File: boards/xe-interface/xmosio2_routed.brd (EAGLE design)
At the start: 116.8 x 55.2 mm, 105 parts, among them IC1 IDTQS3245QSOP20, IC2 IDTQS3245QSOP20, IC3 IDTQS3245QSOP20, IC4 IDTQS3245QSOP20, IC5 IDTQS3245QSOP20, U1 24 MHz Osc. (F535L-24), U2 USD-SOCKETNEW, X1 0446200002

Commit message: Latest board (routed and unrolled)
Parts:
- added GPIO: (no value), pinhead:1X04
- added H1, H2, H3, H4: MOUNT-HOLE3.2, holes:3,2
- added LED2: ok33, led:CHIP-LED0805
- added MEM_SEL: (no value), special:EDG-02
- added PBI_ID: (no value), special:EDG-03
- added R28: 47R, rcl:R1206
- added R29, R30, R31, R33, R34: 10K, rcl:R1206
- added SJ2, SJ3: SOLDERJUMPERNO, SparkFun:SJ_2S-NO
- added U$19: XE_SLOT, pbxl:XE_SLOT
- C1, C2, C3, C4, C5: device rcl:C0805 -> rcl:C1206
- C10, C11, C12, C13, C14, C15, C16, C17, C18, C19, C20, C21, C22, C23, C24, C25, C26, C28, C31, C34, C35, C36, C37, C38, C39, C40, C41, C42, C43, C44, C45, C46, C6, C7, C8, C9: device rcl:C0603 -> rcl:C1206
- R1, R10, R11, R12, R13, R14, R15, R16, R17, R18, R19, R2, R20, R21, R22, R23, R24, R25, R26, R27, R3, R4, R5, R6, R7, R8, R9: device rcl:R0603 -> rcl:R1206
- moved DBG3 116.3 mm to (113.7, 69.8), turned to 90 degrees
- moved DBG2 115.9 mm to (113.7, 66.7), turned to 90 degrees
- moved DBG1 115.6 mm to (113.7, 63.5), turned to 90 degrees
- moved DBG0 115.2 mm to (113.7, 60.3), turned to 90 degrees
- moved R23 101.1 mm to (108.6, 69.8), turned to 180 degrees
- moved R22 97.4 mm to (108.6, 66.7), turned to 180 degrees
- moved R21 93.8 mm to (108.6, 63.5), turned to 180 degrees
- moved U$10 93.7 mm to (23.9, 54.1), turned to 90 degrees
- moved R10 93.4 mm to (23.4, 59.9), turned to 0 degrees
- moved R20 90.1 mm to (108.6, 60.3), turned to 180 degrees
- moved U$9 87.2 mm to (34.2, 51.5), turned to 90 degrees
- moved R11 86.4 mm to (23.4, 47.9), turned to 0 degrees
- moved R8 79.8 mm to (22.6, 38.6), turned to 90 degrees
- moved C40 77.3 mm to (22.6, 31.7), turned to 90 degrees
- moved C39 76.1 mm to (22.6, 23.4), turned to 270 degrees
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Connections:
- new net N$30: C29.+, L1.1, LED1.A, R3.2, SJ2.1
- new net N$31: LED2.C, R28.2
- new net N$32: C32.+, L2.1, LED2.A, R6.2, SJ3.1
- new net N$34: MEM_SEL.2, R29.1, U$2.25
- new net N$35: MEM_SEL.1, R30.2, U$2.26
- new net N$36: GPIO.3, U$2.12
- new net N$37: GPIO.2, U$2.14
- new net PBI0: PBI_ID.1, R31.2, U$2.33
- new net PBI1: PBI_ID.2, R34.2, U$2.61
- new net PBI2: PBI_ID.3, R33.2, U$2.62
- net +5V: now also U$19.26, U$19.44
- net B1: now also U$19.1
- net B10: now also U$19.11
- net B11: now also U$19.12
- net B12: now also U$19.13
- net B13: now also U$19.14
- net B14: now also U$19.15
- net B15: now also U$19.16
- net B16: now also U$19.17
- net B17: now also U$19.18
- net B18: now also U$19.19
- net B19: now also U$19.20
- net B2: now also U$19.2
- net B20: now also U$19.21
- net B21: now also U$19.22
- net B22: now also U$19.23
- net B23: now also U$19.24
- net B24: now also U$19.25
- net B25: now also U$19.27
- net B26: now also U$19.28
- net B27: now also U$19.29
- net B28: now also U$19.30
- net B29: now also U$19.32
- net B3: now also U$19.4
- net B30: now also U$19.33
- net B31: now also U$19.34
- net B32: now also U$19.35
- net B33: now also U$19.36
- net B34: now also U$19.37
- net B35: now also U$19.38
- net B36: now also U$19.39
- net B37: now also U$19.41
- net B38: now also U$19.42
- net B4: now also U$19.5
- net B5: now also U$19.6
- net B6: now also U$19.7
- net B7: now also U$19.8
- net B8: now also U$19.9
- net B9: now also U$19.10
- net GND: now also GPIO.1, R28.1, R29.2, R30.1, R31.1, R33.1, R34.1, U$19.3, U$19.43
- net VCCINT: now also SJ3.2; no longer C32.+, L2.1, R6.2, U$6.5
- net VCCIO: now also GPIO.4, MEM_SEL.3, MEM_SEL.4, PBI_ID.4, PBI_ID.5, PBI_ID.6, SJ2.2, U$6.5; no longer C29.+, L1.1, LED1.A, R3.2
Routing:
- net VCCIO: track 456.0 -> 256.4 mm, vias 10 -> 29
- net +5V: track 145.0 -> 238.6 mm, vias 1 -> 2
- net SDC_D1: track 64.5 -> 155.1 mm
- net GND: track 464.6 -> 551.5 mm, vias 32 -> 37
- net SDC_CLK: track 69.7 -> 147.2 mm
- net N$33: track 23.3 -> 99.8 mm, vias 1 -> 3
- net N$21: track 22.1 -> 96.7 mm, vias 1 -> 0
- net N$35: track 0.00 -> 74.3 mm, vias 0 -> 3
- net N$36: track 0.00 -> 70.2 mm, vias 0 -> 1
- net N$34: track 0.00 -> 62.0 mm, vias 0 -> 1
- net PBI2: track 0.00 -> 61.1 mm, vias 0 -> 1
- net N$32: track 0.00 -> 56.3 mm
- net VCCINT: track 174.3 -> 228.8 mm, vias 10 -> 4
- net PBI0: track 0.00 -> 54.4 mm, vias 0 -> 1
- net N$30: track 0.00 -> 52.6 mm
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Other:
- board size 116.8 x 55.2 mm -> 116.8 x 100 mm
- board text added: "(c) 2018 SjG"
- board text added: "+1v"
- board text added: "+3.3v"
- board text added: "+5v"
- board text added: "3.3V"
- board text added: "GND"
- board text added: "PGOOD"
- board text added: "XMOS io v2.0"

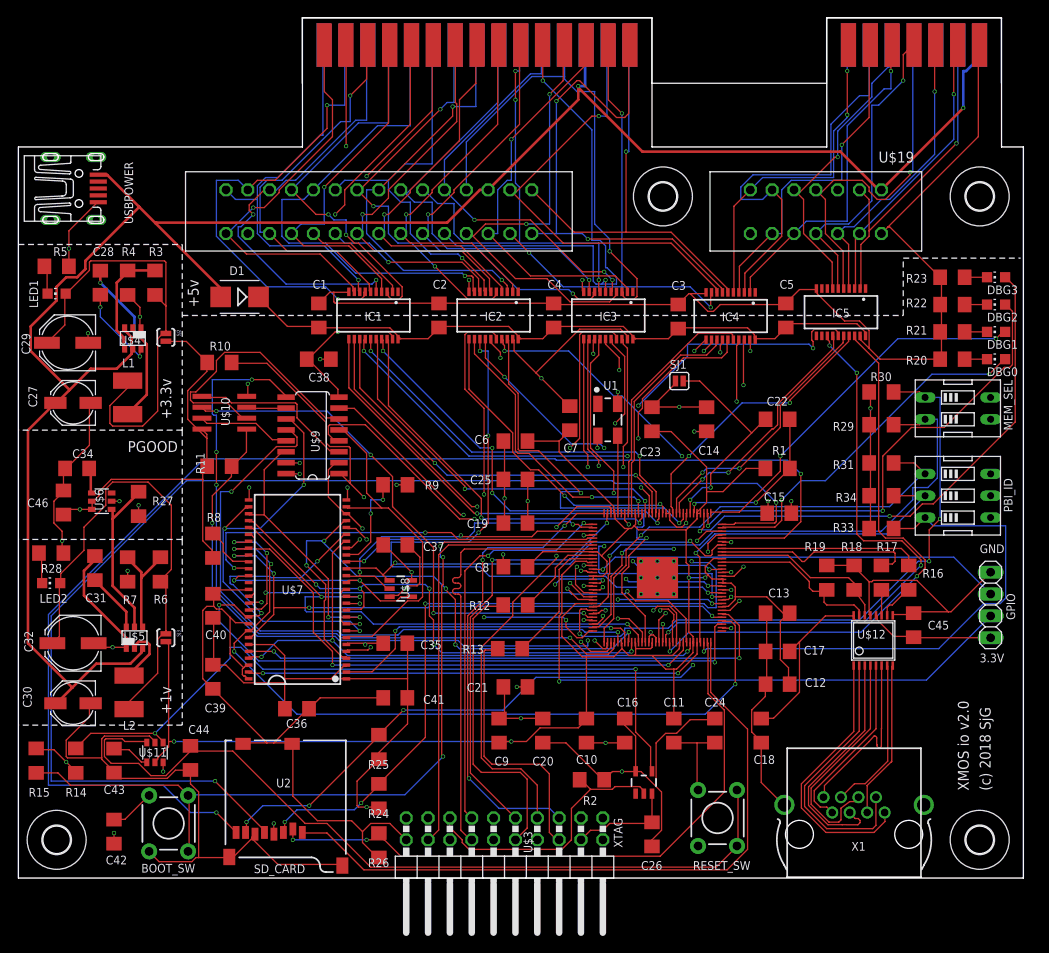
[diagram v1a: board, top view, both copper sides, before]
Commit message: Latest design changes  - Move the XTAG connector back significantly, so the shroud is not overhanging the board  - Use the SD card slot, not the micro-SD card, it’s easier to solder  - Fix the SD card pinouts  - Remove an unwanted pull-up on the SD card
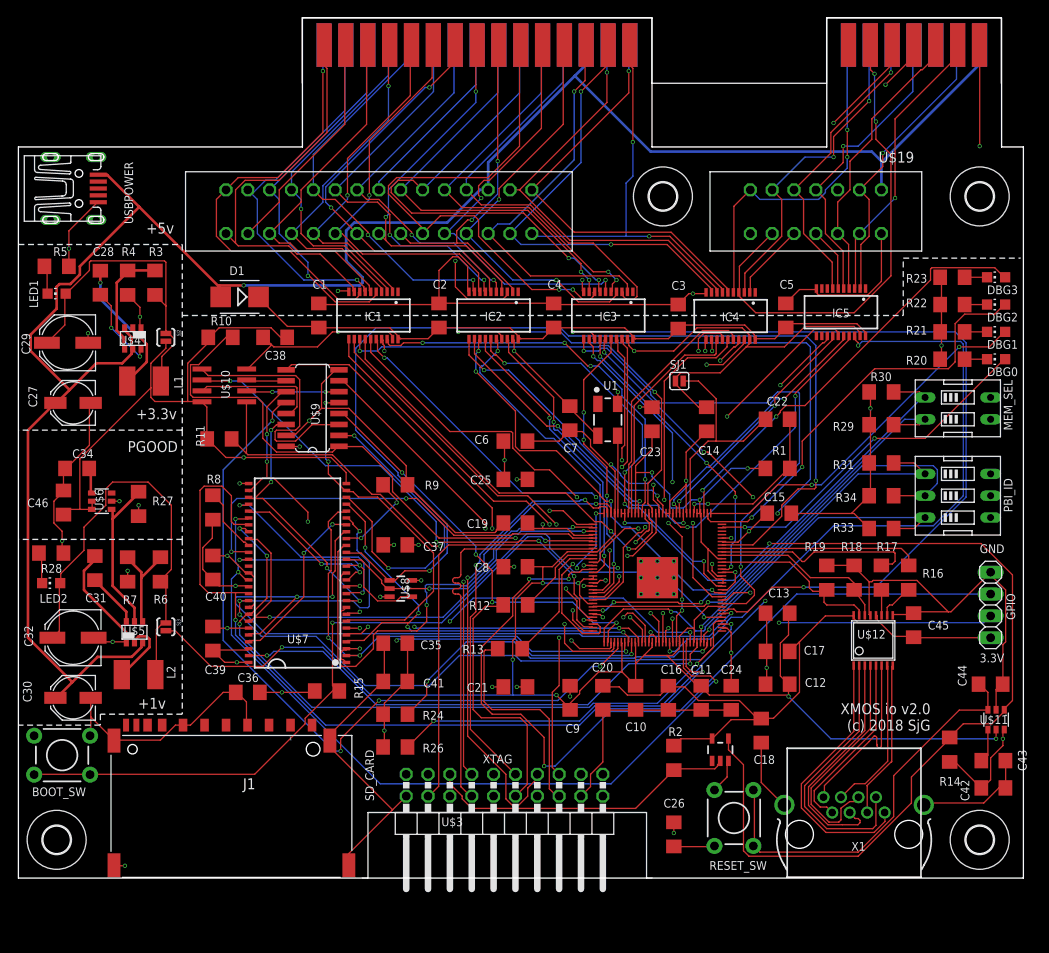
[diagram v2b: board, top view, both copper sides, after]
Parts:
- removed R25: 10K, rcl:R1206
- removed U2: USD-SOCKETNEW, SparkFun-Connectors:MICRO-SD-SOCKET-PP
- added J1: (no value), InputOutputIO (rev17e):693063020911
- moved C42 102.4 mm to (113.3, 10.5), turned to 0 degrees
- moved C43 102.2 mm to (113.3, 13.7), turned to 0 degrees
- moved R14 101.6 mm to (108.3, 14.9)
- moved U$11 97.9 mm to (113.7, 18.4)
- moved C44 93.4 mm to (113.0, 22.5), turned to 180 degrees
- moved R15 34.8 mm to (35.9, 21.7), turned to 180 degrees
- moved BOOT_SW 14.7 mm to (5.08, 14.3), turned to 180 degrees
- moved R26 11.6 mm to (43.8, 15.2), turned to 0 degrees
- moved R2 9.86 mm to (76.2, 14.0), turned to 90 degrees
- moved R24 9.71 mm to (43.8, 19.1), turned to 180 degrees
- moved U$3 9.67 mm to (81.6, 14.9)
- moved C9 9.09 mm to (64.1, 21.0)
- moved C20 7.96 mm to (67.9, 21.0), turned to 270 degrees
- moved C10 6.87 mm to (71.8, 21.0)
- moved C16 6.35 mm to (75.6, 21.0)
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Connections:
- new net SDC_CD: U$2.84
- net GND: now also J1.3, J1.6, J1.GND1, J1.GND2, J1.GND3, J1.GND4; no longer R26.2, U2.6, U2.CD1, U2.CD2, U2.GND1, U2.GND3
- net SDC_CLK: now also U$2.64; no longer U$2.96, U2.5
- net SDC_CMD: now also U$2.63; no longer U$2.94, U2.3
- net SDC_D0: now also U$2.96; no longer R25.1, U$2.93, U2.7
- net SDC_D1: now also U$2.94; no longer U$2.92, U2.8
- net SDC_D2: now also U$2.93; no longer U$2.64, U2.1
- net SDC_D3: now also R26.2, U$2.92; no longer R26.1, U$2.63, U2.2
- net VCCIO: now also R26.1; no longer R25.2, U2.4
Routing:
- net SDC_D1: track 155.1 -> 0.00 mm, vias 2 -> 0
- net SDC_CLK: track 147.2 -> 0.00 mm, vias 2 -> 0
- net !SD_CAS!: track 48.3 -> 128.9 mm
- net SDC_D2: track 80.4 -> 0.00 mm
- net SDC_D0: track 77.7 -> 0.00 mm, vias 5 -> 0
- net X_D0: track 40.0 -> 101.4 mm
- net N$21: track 96.7 -> 47.4 mm
- net N$37: track 48.6 -> 97.4 mm, vias 1 -> 3
- net SDC_CMD: track 85.1 -> 41.1 mm, vias 5 -> 2
- net X_D2: track 47.2 -> 82.4 mm
- net X_D4: track 77.0 -> 46.8 mm
- net SD_ADQ9: track 67.8 -> 97.6 mm, vias 4 -> 2
- net SD_ADQ4/QS_D2: track 84.7 -> 57.7 mm, vias 4 -> 2
- net VCCINT: track 228.8 -> 254.1 mm, vias 4 -> 11
- net PBI2: track 61.1 -> 36.6 mm
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
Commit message: Add a new progress post
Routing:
- net !SD_CAS!: track 128.9 -> 49.6 mm, vias 2 -> 3
- net X_RD4: track 54.6 -> 120.7 mm
- net X_D0: track 101.4 -> 43.8 mm
- net VCCINT: track 254.1 -> 305.2 mm, vias 11 -> 16
- net N$34: track 51.6 -> 102.2 mm
- net !X_S4!: track 51.9 -> 99.3 mm
- net N$37: track 97.4 -> 52.5 mm, vias 3 -> 1
- net X_D2: track 82.4 -> 43.5 mm, vias 3 -> 2
- net !RESET!: track 122.3 -> 87.7 mm
- net VCCIO: track 272.5 -> 244.3 mm, vias 24 -> 30
- net X_A8: track 33.7 -> 61.6 mm
- net SD_ADQ8: track 93.0 -> 68.3 mm, vias 3 -> 2
- net X_D1: track 61.1 -> 39.3 mm
- net SD_ADQ5/QS_D3: track 88.7 -> 67.7 mm, vias 4 -> 2
- net QSPI_CLK: track 60.3 -> 81.2 mm, vias 4 -> 2
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
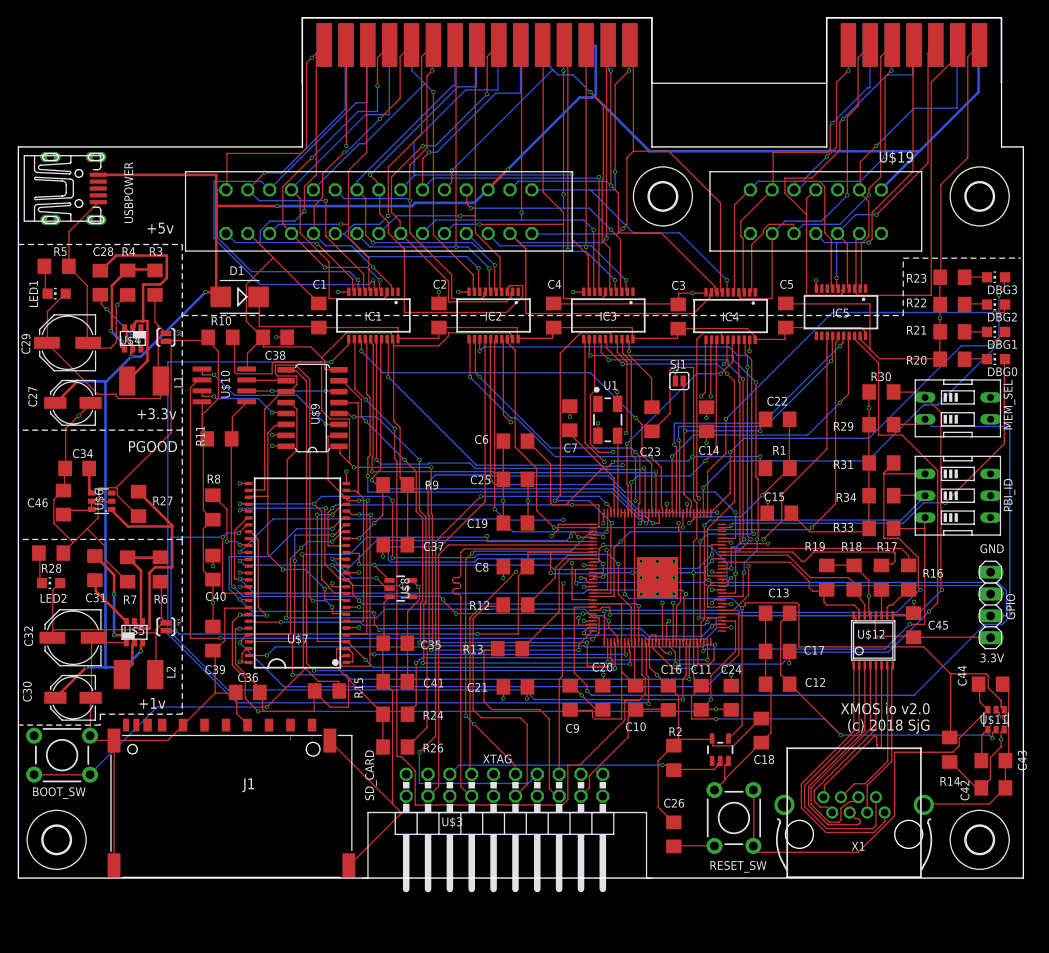
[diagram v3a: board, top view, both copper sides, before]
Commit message: Update the routed and unrouted board files, delete an unwanted routed-board file
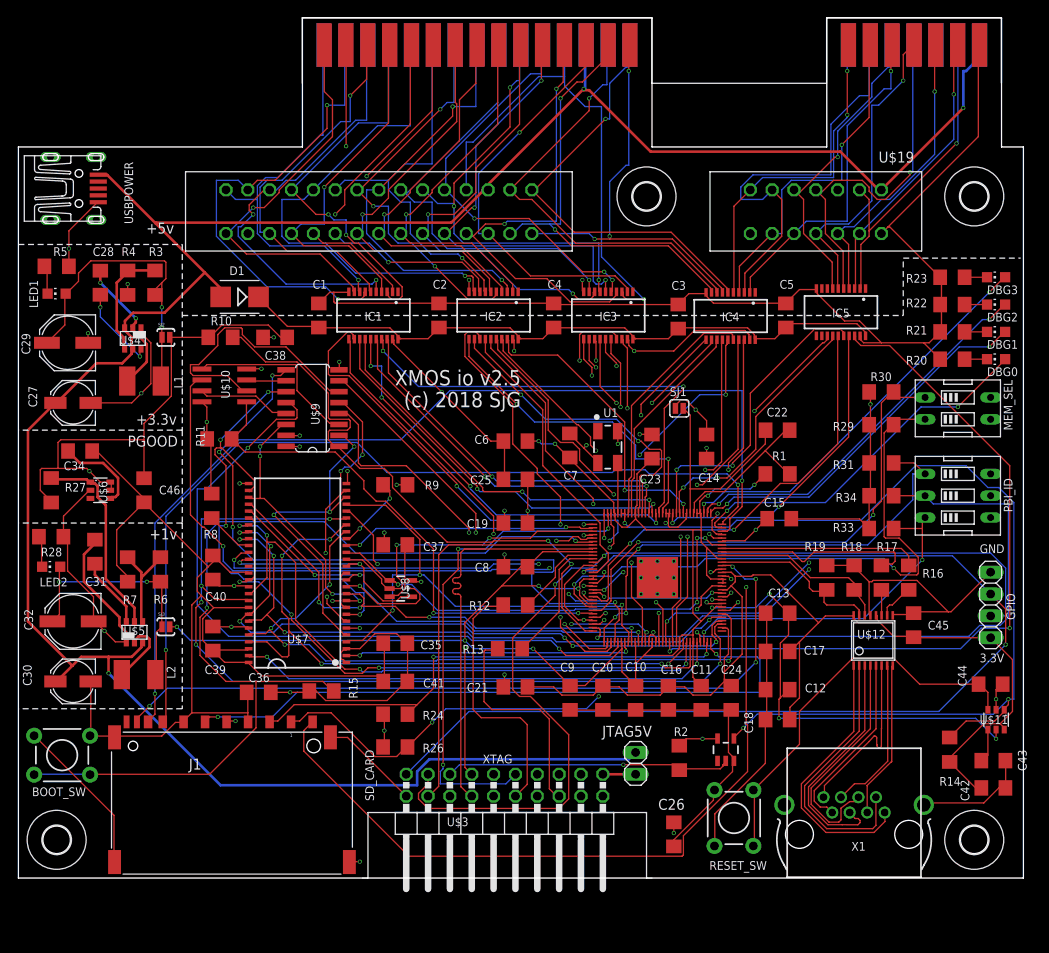
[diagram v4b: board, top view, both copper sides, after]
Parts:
- added JTAG5V: PSU, pinhead:1X02
- GPIO: value (none) -> UART
- J1: value (none) -> SD_CARD
- MEM_SEL: value (none) -> CT2092MS-ND
- PBI_ID: value (none) -> CT2093MS-ND
- moved R27 10.3 mm to (3.81, 45.1)
- moved C46 9.47 mm to (14.6, 45.1), turned to 270 degrees
- moved C14 3.18 mm to (80.0, 50.2)
- moved C23 3.18 mm to (73.7, 50.2)
- moved C7 3.17 mm to (64.1, 50.3)
- moved SJ1 3.17 mm to (76.8, 54.6)
- moved U1 3.17 mm to (68.5, 50.1)
- moved C18 2.29 mm to (88.3, 18.4), turned to 180 degrees
- moved C34 2.05 mm to (7.17, 49.6), turned to 0 degrees
- moved C30 1.91 mm to (6.35, 22.9)
- moved H3 1.91 mm to (73.0, 79.2)
- moved LED2 1.91 mm to (3.81, 36.2)
- moved R28 1.91 mm to (3.81, 39.7)
- moved C32 1.90 mm to (6.35, 29.8)
- moved C31 1.90 mm to (8.89, 37.9)
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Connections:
- net N$21 renamed TRST_N
- removed net N$36: GPIO.3, U$2.12
- removed net N$37: GPIO.2, U$2.14
- new net N$38: JTAG5V.2, XTAG.1
- new net UART_RX: GPIO.2, U$2.14, XTAG.19
- new net UART_TX: GPIO.3, U$2.12, XTAG.17
- net +5V: now also JTAG5V.1
- net SDC_CD: now also J1.CD
- net SDC_CLK: now also J1.5
- net SDC_CMD: now also J1.2
- net SDC_D0: now also J1.7
- net SDC_D1: now also J1.8
- net SDC_D2: now also J1.9
- net SDC_D3: now also J1.1
- net VCCIO: now also J1.4
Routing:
- net UART_RX: track 0.00 -> 133.7 mm, vias 0 -> 2
- net SDC_D1: track 0.00 -> 115.8 mm, vias 0 -> 2
- net UART_TX: track 0.00 -> 115.7 mm, vias 0 -> 2
- net SDC_D0: track 0.00 -> 101.9 mm, vias 0 -> 2
- net SDC_D2: track 0.00 -> 100.9 mm, vias 0 -> 2
- net SDC_CD: track 0.00 -> 89.3 mm, vias 0 -> 4
- net SDC_CLK: track 0.00 -> 76.7 mm, vias 0 -> 2
- net +5V: track 221.5 -> 289.6 mm, vias 7 -> 3
- net X_RD4: track 120.7 -> 54.2 mm, vias 2 -> 3
- net VCCINT: track 305.2 -> 246.4 mm, vias 16 -> 13
- net N$36: track 58.1 -> 0.00 mm, vias 1 -> 0
- net GND: track 531.9 -> 586.4 mm, vias 41 -> 37
- net N$37: track 52.5 -> 0.00 mm, vias 1 -> 0
- net VCCIO: track 244.3 -> 295.8 mm, vias 30 -> 23
- net !X_S4!: track 99.3 -> 64.3 mm, vias 2 -> 3
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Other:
- board text added: "XMOS io v2.5"
- board text removed: "XMOS io v2.0"

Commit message: Latest board files. Submitted board is xmosio2_routed.brd
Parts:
- removed D1: MURS120-E3, diode:SMB
- added D2: (no value), SparkFun-DiscreteSemi:DIODE-1N4001-KIT
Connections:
- net +4.3V: now also D2.C; no longer D1.C
- net +5V: now also D2.A; no longer D1.A
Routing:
- net GND: track 586.4 -> 610.0 mm, vias 37 -> 34
- net X_D6: track 36.2 -> 52.5 mm, vias 2 -> 3
- net X_D3: track 37.9 -> 50.7 mm, vias 2 -> 3
- net VCCIO: track 295.8 -> 283.6 mm, vias 23 -> 24
- net SDC_CLK: track 76.7 -> 66.6 mm
- net !X_S4!: track 64.3 -> 57.7 mm, vias 3 -> 4
- net !SD_CAS!: track 54.8 -> 60.6 mm, vias 4 -> 3
- net SDC_CD: track 89.3 -> 85.9 mm
- net +5V: track 289.6 -> 286.4 mm
- net +4.3V: track 78.9 -> 75.9 mm
- net X_A8: track 34.1 -> 37.1 mm, vias 0 -> 2
- net !X_S5!: track 40.9 -> 38.0 mm
- net VCCINT: track 246.4 -> 243.6 mm
- net TDI: track 33.5 -> 35.6 mm
- net SDC_D1: track 115.8 -> 117.8 mm
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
